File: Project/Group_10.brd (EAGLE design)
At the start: 73.7 x 48.3 mm, 29 parts, among them J1 POWER_JACKPTH_LOCK, U1 +12v, U3 TCA9546ASO16, U4 TMUX1208

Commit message: Added M3 holes
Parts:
- moved J1 4.03 mm to (-1.63, 54.8)
- moved J5 1.98 mm to (-64.2, 91.4)
- moved J2 1.98 mm to (-14.7, 91.4)
- moved J4 1.98 mm to (-56.5, 91.4)
- moved R4 1.98 mm to (-51.5, 89.0)
- moved R5 1.98 mm to (-59.1, 89.0)
- moved R6 1.98 mm to (-69.3, 89.0)
- moved R7 1.98 mm to (-61.7, 89.0)
- moved R8 1.98 mm to (-22.3, 89.0)
- moved U3 1.98 mm to (-41.4, 90.2)
- moved J7 1.98 mm to (-9.73, 91.5)
- moved R3 1.98 mm to (-12.1, 89.0)
- moved J3 1.98 mm to (-27.4, 91.4)
- moved R2 1.98 mm to (-19.8, 89.0)
- moved R9 1.98 mm to (-29.9, 89.0)
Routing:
- net N$1: track 45.5 -> 47.8 mm
- net I2C_A0: track 19.1 -> 21.1 mm
- net I2C_A1: track 21.4 -> 23.4 mm
- net I2C_A2: track 22.9 -> 24.9 mm
- net 5V: track 67.3 -> 66.4 mm
- net I2C_SCL: track 7.77 -> 8.65 mm
- net I2C_SDA: track 5.85 -> 6.72 mm

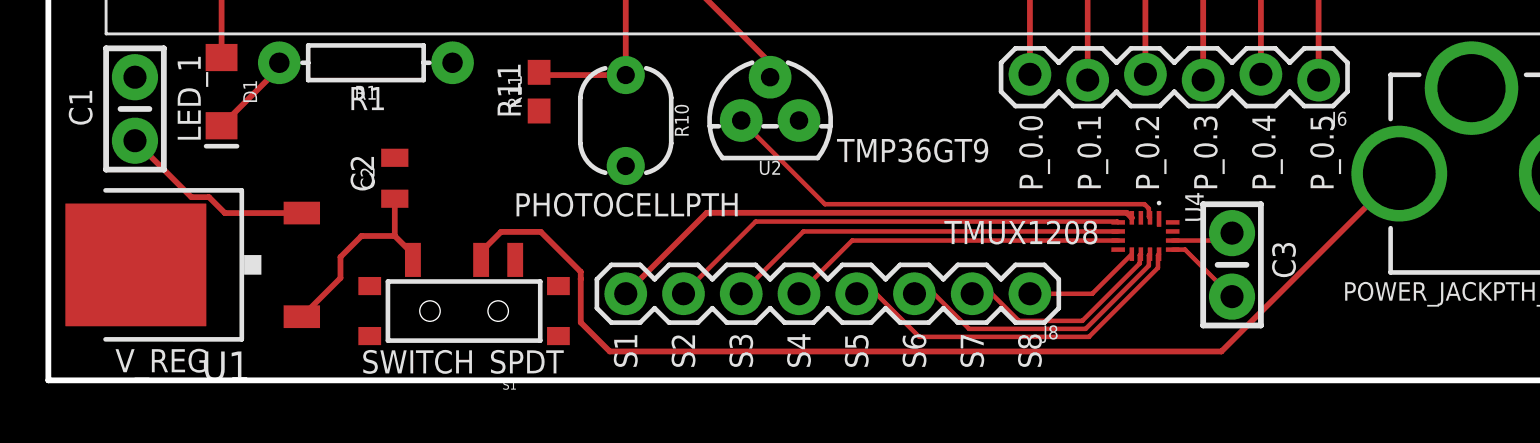
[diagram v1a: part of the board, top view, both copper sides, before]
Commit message: Increased width of power traces for possible current requirements
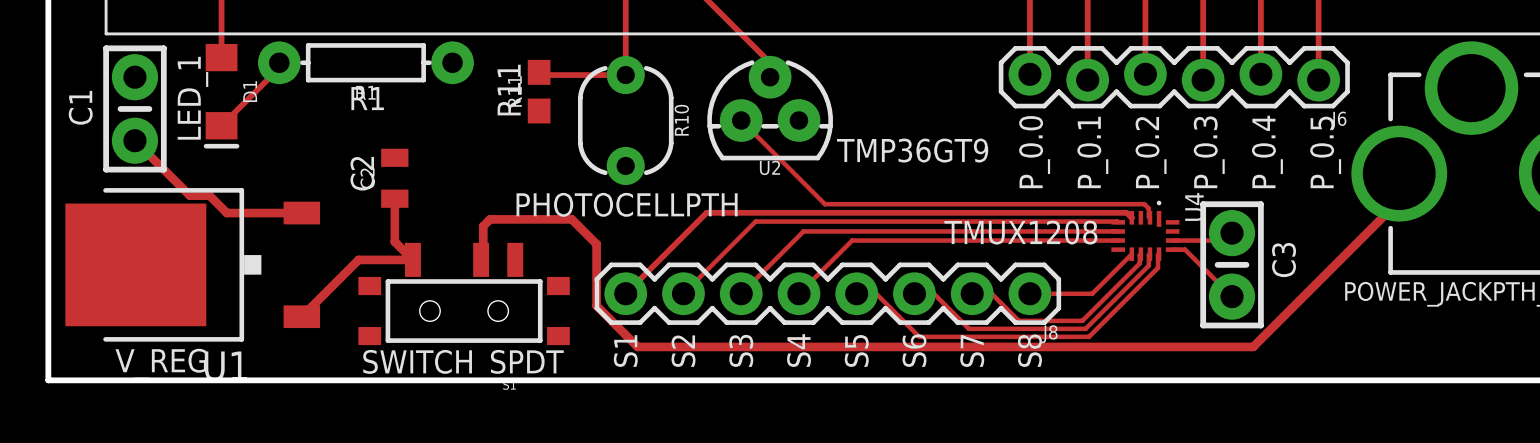
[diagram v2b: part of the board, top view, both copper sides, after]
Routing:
- net N$1: track 47.8 -> 49.7 mm
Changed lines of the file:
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@@
 <setting verticaltext="up"/>
 </settings>
-<grid distance="0.3" unitdist="mm" unit="mm" style="lines" multiple="1" display="yes" altdistance="2" altunitdist="mil" altunit="mil"/>
+<grid distance="11.8110236" unitdist="mil" unit="mil" style="lines" multiple="1" display="yes" altdistance="2" altunitdist="mil" altunit="mil"/>
 <layers>
 <layer number="1" name="Top" color="4" fill="1" visible="yes" active="yes"/>
@@
 <contactref element="J1" pad="PWR"/>
 <contactref element="S1" pad="P"/>
-<wire x1="-15.5034" y1="54.8132" x2="-23.3266" y2="46.99" width="0.254" layer="1"/>
-<wire x1="-23.3266" y1="46.99" x2="-50.23353125" y2="46.99" width="0.254" layer="1"/>
-<wire x1="-51.5094" y1="50.18053125" x2="-51.5112" y2="50.18233125" width="0.254" layer="1"/>
-<wire x1="-51.5112" y1="50.18233125" x2="-51.5112" y2="50.4952" width="0.254" layer="1"/>
-<wire x1="-50.23353125" y1="46.99" x2="-51.5094" y2="48.26586875" width="0.254" layer="1"/>
-<wire x1="-51.5094" y1="48.26586875" x2="-51.5094" y2="50.18053125" width="0.254" layer="1"/>
-<wire x1="-51.5112" y1="50.4952" x2="-53.2666" y2="52.2506" width="0.254" layer="1"/>
-<wire x1="-53.2666" y1="52.2506" x2="-55.015" y2="52.2506" width="0.254" layer="1"/>
-<wire x1="-55.015" y1="52.2506" x2="-55.892" y2="51.3736" width="0.254" layer="1"/>
-<wire x1="-55.892" y1="51.3736" x2="-55.892" y2="51.018" width="0.254" layer="1"/>
+<wire x1="-55.892" y1="51.018" x2="-55.8" y2="51.11" width="0.381" layer="1"/>
+<wire x1="-55.8" y1="51.11" x2="-55.8" y2="52.5" width="0.381" layer="1"/>
+<wire x1="-55.8" y1="52.5" x2="-55.5" y2="52.8" width="0.381" layer="1"/>
+<wire x1="-55.5" y1="52.8" x2="-51.9" y2="52.8" width="0.381" layer="1"/>
+<wire x1="-50.8127" y1="48.9986875" x2="-49.0041125" y2="47.1901" width="0.381" layer="1"/>
+<wire x1="-51.9" y1="52.8" x2="-50.8127" y2="51.7127" width="0.381" layer="1"/>
+<wire x1="-50.8127" y1="51.7127" x2="-50.8127" y2="48.9986875" width="0.381" layer="1"/>
+<wire x1="-49.0041125" y1="47.1901" x2="-21.9265" y2="47.1901" width="0.381" layer="1"/>
+<wire x1="-15.5034" y1="53.6132" x2="-21.9265" y2="47.1901" width="0.381" layer="1"/>
+<wire x1="-15.5034" y1="53.6132" x2="-15.5034" y2="54.8132" width="0.381" layer="1"/>
 </signal>
 <signal name="GND">
@@
 <contactref element="S1" pad="O"/>
 <contactref element="U1" pad="1"/>
-<wire x1="-59.69" y1="53.71" x2="-59.69" y2="52.07" width="0.254" layer="1"/>
-<wire x1="-63.78" y1="48.52" x2="-62.0794" y2="50.2206" width="0.254" layer="1"/>
-<wire x1="-62.0794" y1="50.2206" x2="-62.0794" y2="51.14573125" width="0.254" layer="1"/>
-<wire x1="-62.0794" y1="51.14573125" x2="-61.15513125" y2="52.07" width="0.254" layer="1"/>
-<wire x1="-61.15513125" y1="52.07" x2="-59.69" y2="52.07" width="0.254" layer="1"/>
-<wire x1="-59.69" y1="52.07" x2="-58.892" y2="51.272" width="0.254" layer="1"/>
-<wire x1="-58.892" y1="51.272" x2="-58.892" y2="51.018" width="0.254" layer="1"/>
+<wire x1="-63.78" y1="48.52" x2="-61.282" y2="51.018" width="0.381" layer="1"/>
+<wire x1="-61.282" y1="51.018" x2="-58.892" y2="51.018" width="0.381" layer="1"/>
+<wire x1="-59.69" y1="51.816" x2="-59.69" y2="53.71" width="0.381" layer="1"/>
+<wire x1="-58.892" y1="51.018" x2="-59.69" y2="51.816" width="0.381" layer="1"/>
 </signal>
 <signal name="5V">
@@
 <wire x1="-29.9212" y1="88.1008" x2="-22.3012" y2="88.1008" width="0.254" layer="1"/>
 <wire x1="-22.3012" y1="88.1008" x2="-19.7612" y2="88.1008" width="0.254" layer="1"/>
-<wire x1="-71.12" y1="56.261" x2="-68.6384" y2="53.7794" width="0.254" layer="1"/>
-<wire x1="-68.6384" y1="53.7794" x2="-67.86426875" y2="53.7794" width="0.254" layer="1"/>
-<wire x1="-67.16486875" y1="53.08" x2="-63.78" y2="53.08" width="0.254" layer="1"/>
-<wire x1="-67.86426875" y1="53.7794" x2="-67.16486875" y2="53.08" width="0.254" layer="1"/>
 <polygon width="0.254" layer="16" isolate="0.2032">
 <vertex x="-74.93" y="45.72"/>
@@
 <wire x1="-12.1412" y1="88.1008" x2="-10.5782" y2="88.1008" width="0.254" layer="1"/>
 <wire x1="-10.5782" y1="88.1008" x2="-9.7282" y2="88.9508" width="0.254" layer="1"/>
+<wire x1="-67.83796875" y1="53.8429" x2="-68.7019" y2="53.8429" width="0.381" layer="1"/>
+<wire x1="-68.7019" y1="53.8429" x2="-71.12" y2="56.261" width="0.381" layer="1"/>
+<wire x1="-63.78" y1="53.08" x2="-67.07506875" y2="53.08" width="0.381" layer="1"/>
+<wire x1="-67.07506875" y1="53.08" x2="-67.83796875" y2="53.8429" width="0.381" layer="1"/>
 </signal>
 <signal name="PHOTO_OUT">
